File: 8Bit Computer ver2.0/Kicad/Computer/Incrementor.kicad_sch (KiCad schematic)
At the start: 13 parts, among them IC139 SN74ABT245BDWR, IC16 SN74F283D, IC42 SN74F283D, IC43 SN74AHC74DR, IC50 SN74LVC1G14DBVR, IC51 SN74LVC1G32DBVR, IC58 SN74LVC1G08DBVR, IC81 SN74F283D, IC82 SN74LVC1G14DBVR, IC83 SN74LVC1G14DBVR, IC84 SN74LVC1G86DBVR, IC87 SN74ABT574ADWR, IC88 SN74ABT574ADWR

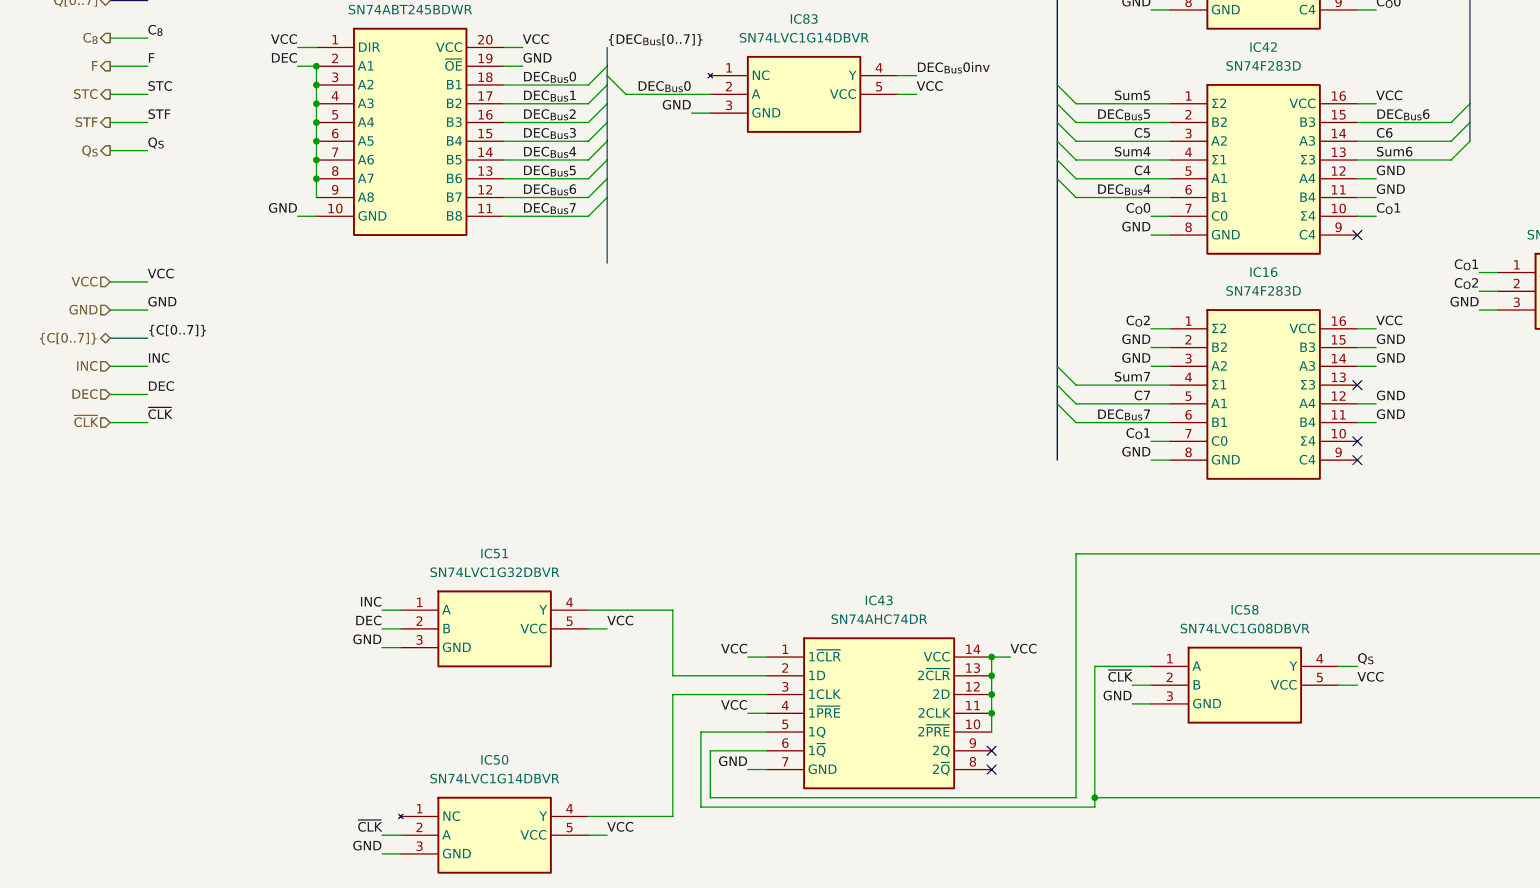
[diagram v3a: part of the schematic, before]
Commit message: Kicad
deleted the Qs
began with FlashMemory
added the CMD comparators for Inc, Comp, AddSub, FlagReg, BarrelShifter, ProgCount
added Diodes and DATdis line
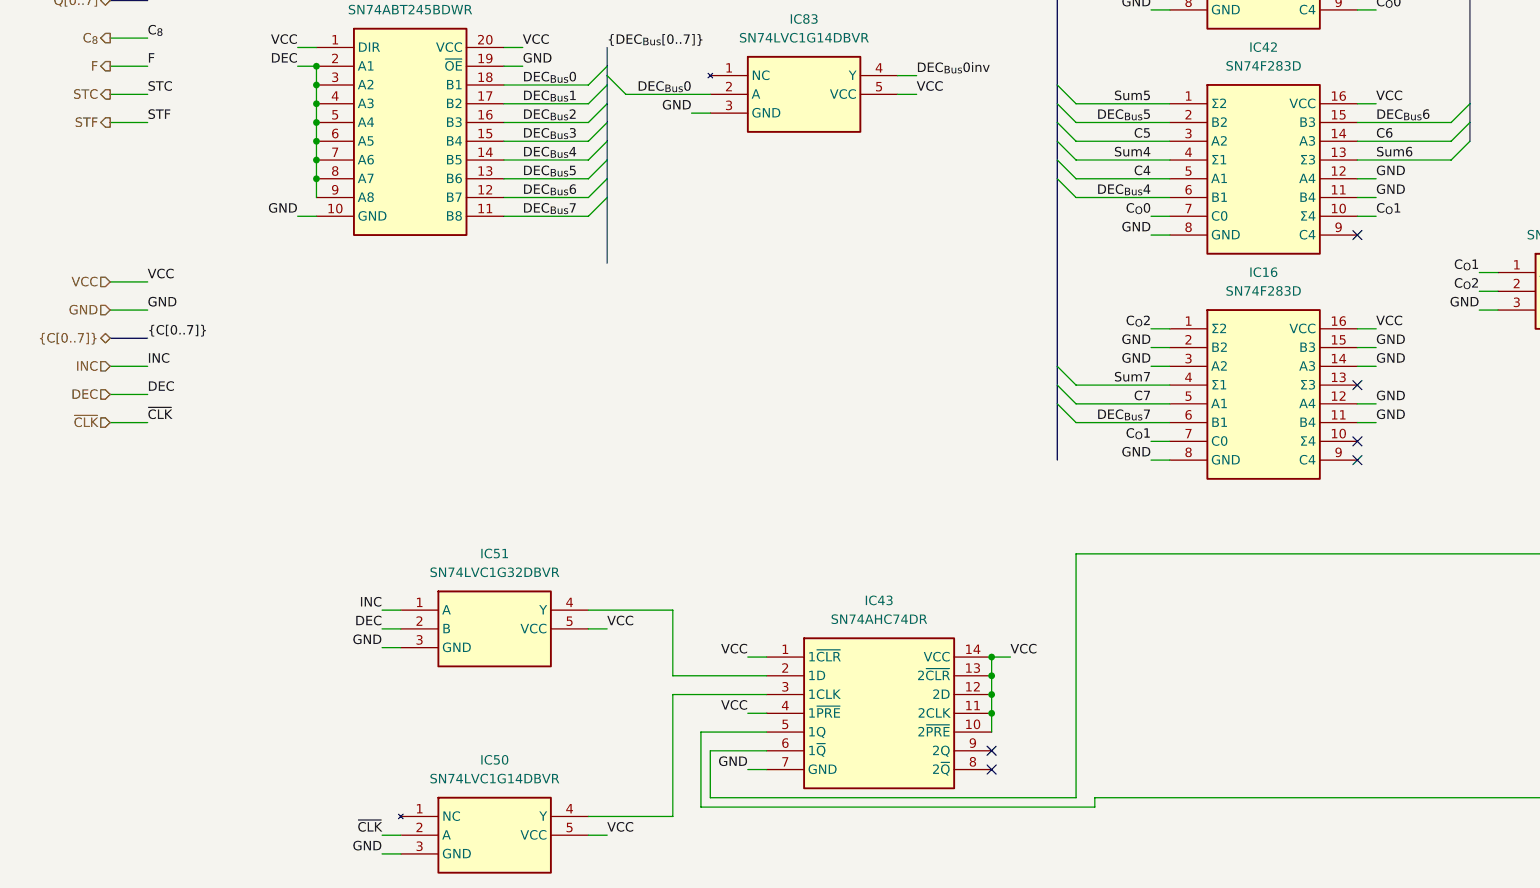
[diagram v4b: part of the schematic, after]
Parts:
- removed IC58: SN74LVC1G08DBVR, Samacsys:SOT95P280X145-5N, symbol Samacsys:SN74LVC1G08DBVR

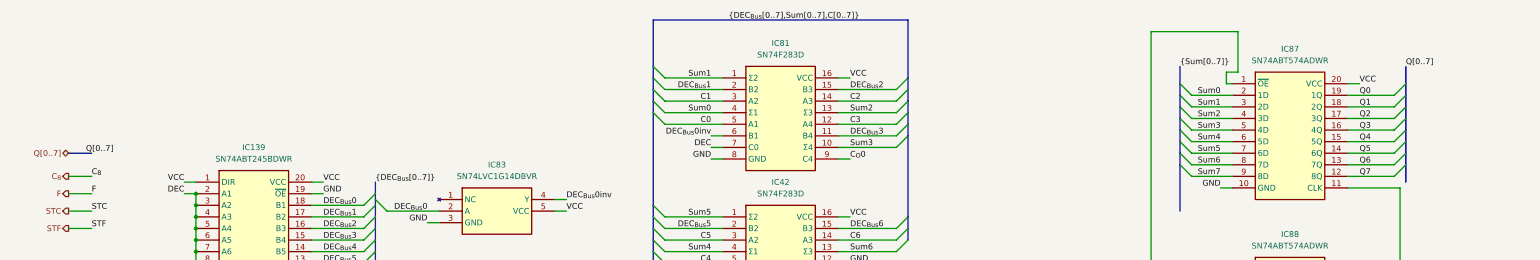
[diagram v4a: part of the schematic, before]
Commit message: Kicad, parts
Parts:
added Leds
Kicad:
added Input Output
changed Q bus to DAT bus
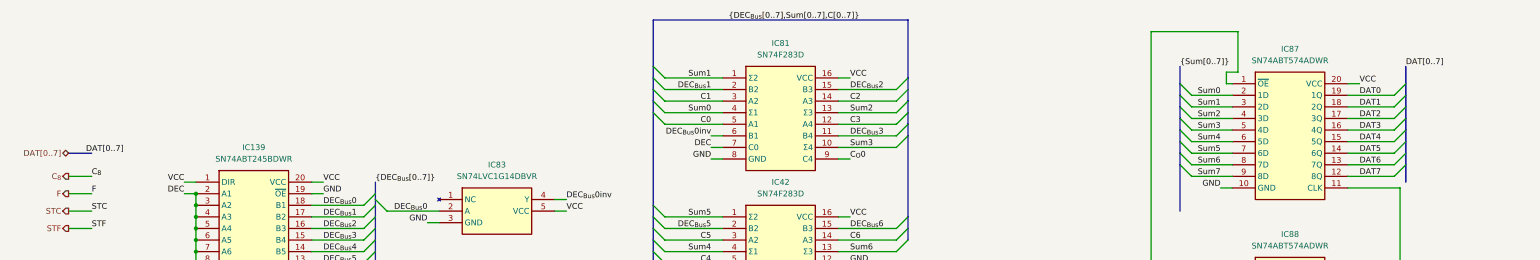
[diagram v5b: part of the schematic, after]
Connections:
- net Q0 renamed DAT0
- net Q1 renamed DAT1
- net Q2 renamed DAT2
- net Q3 renamed DAT3
- net Q4 renamed DAT4
- net Q5 renamed DAT5
- net Q6 renamed DAT6
- net Q7 renamed DAT7
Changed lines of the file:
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@@
 		)
 	)
-	(label "Q5"
+	(label "DAT5"
 		(at 306.07 60.96 0)
 		(effects
@@
 		)
 	)
-	(label "Q1"
+	(label "DAT1"
 		(at 306.07 50.8 0)
 		(effects
@@
 		)
 	)
-	(label "Q7"
+	(label "DAT7"
 		(at 306.07 66.04 0)
 		(effects
@@
 		)
 	)
-	(label "Q4"
+	(label "DAT4"
 		(at 306.07 58.42 0)
 		(effects
@@
 		)
 	)
-	(label "Q3"
+	(label "DAT3"
 		(at 306.07 55.88 0)
 		(effects
@@
 		)
 	)
-	(label "Q0"
+	(label "DAT0"
 		(at 306.07 48.26 0)
 		(effects
@@
 		)
 	)
-	(label "Q[0..7]"
+	(label "DAT[0..7]"
 		(at 316.23 41.91 0)
 		(effects
@@
 		)
 	)
-	(label "Q6"
+	(label "DAT6"
 		(at 306.07 63.5 0)
 		(effects
@@
 		)
 	)
-	(label "Q[0..7]"
+	(label "DAT[0..7]"
 		(at 26.67 60.96 0)
 		(effects
@@
 		)
 	)
-	(label "Q2"
+	(label "DAT2"
 		(at 306.07 53.34 0)
 		(effects
@@
 		)
 	)
-	(hierarchical_label "Q[0..7]"
+	(hierarchical_label "DAT[0..7]"
 		(shape tri_state)
 		(at 22.86 60.96 180)

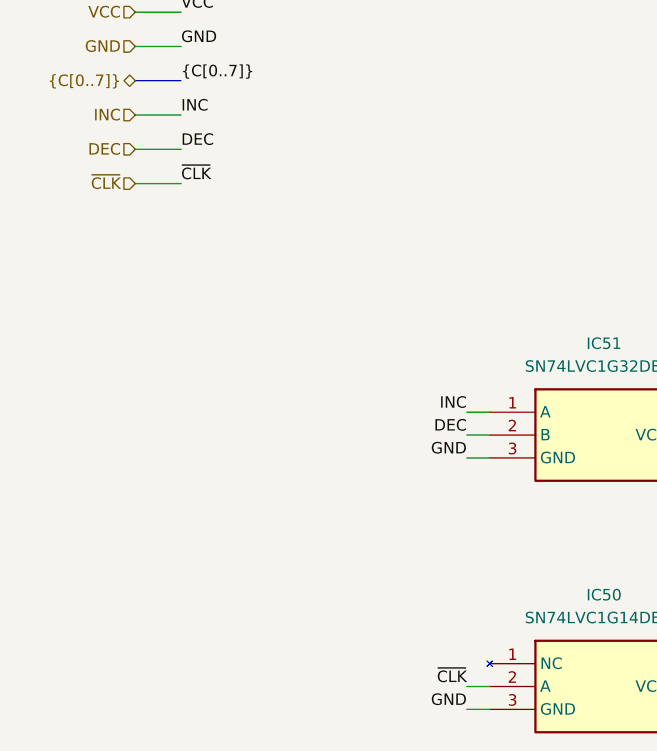
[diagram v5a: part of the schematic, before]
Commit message: Kicad, parts
parts:
added USB C PD Triggerboard
added Delay Chip for 90ns
added Push Button
Kicad:
added USB C PD Triggerboard
added rising edge detector via Delay and Xor for Accept Push Button
added VBUS net
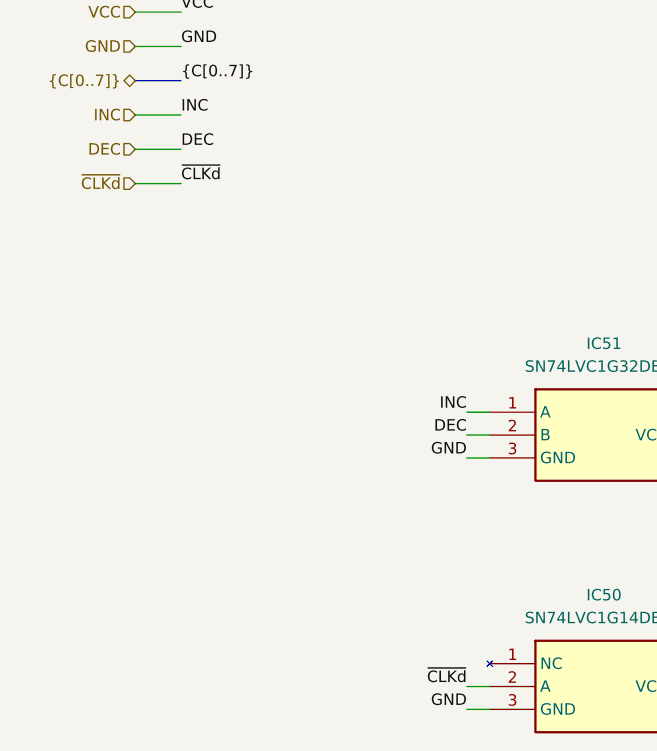
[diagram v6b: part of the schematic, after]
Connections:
- net ~{CLK} renamed ~{CLKd}
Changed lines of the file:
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@@
 		)
 	)
-	(label "~{CLK}"
+	(label "~{CLKd}"
 		(at 59.69 173.99 180)
 		(effects
@@
 		)
 	)
-	(label "~{CLK}"
+	(label "~{CLKd}"
 		(at 27.94 118.11 0)
 		(effects
@@
 		)
 	)
-	(hierarchical_label "~{CLK}"
+	(hierarchical_label "~{CLKd}"
 		(shape input)
 		(at 22.86 118.11 180)

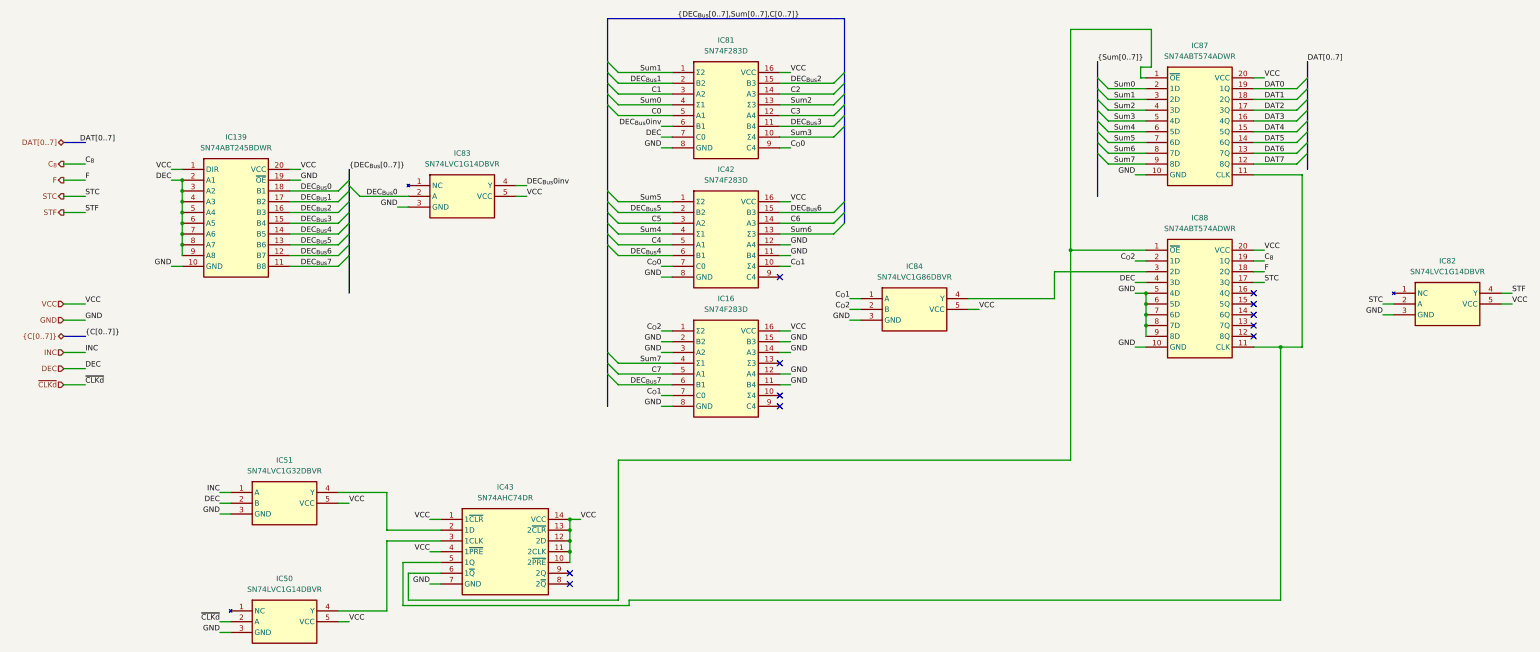
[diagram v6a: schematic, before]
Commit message: Kicad SCH/PCB
Kicad SCH/PCB:
changed the References in SCH
began with INOUTPUT module nearly done
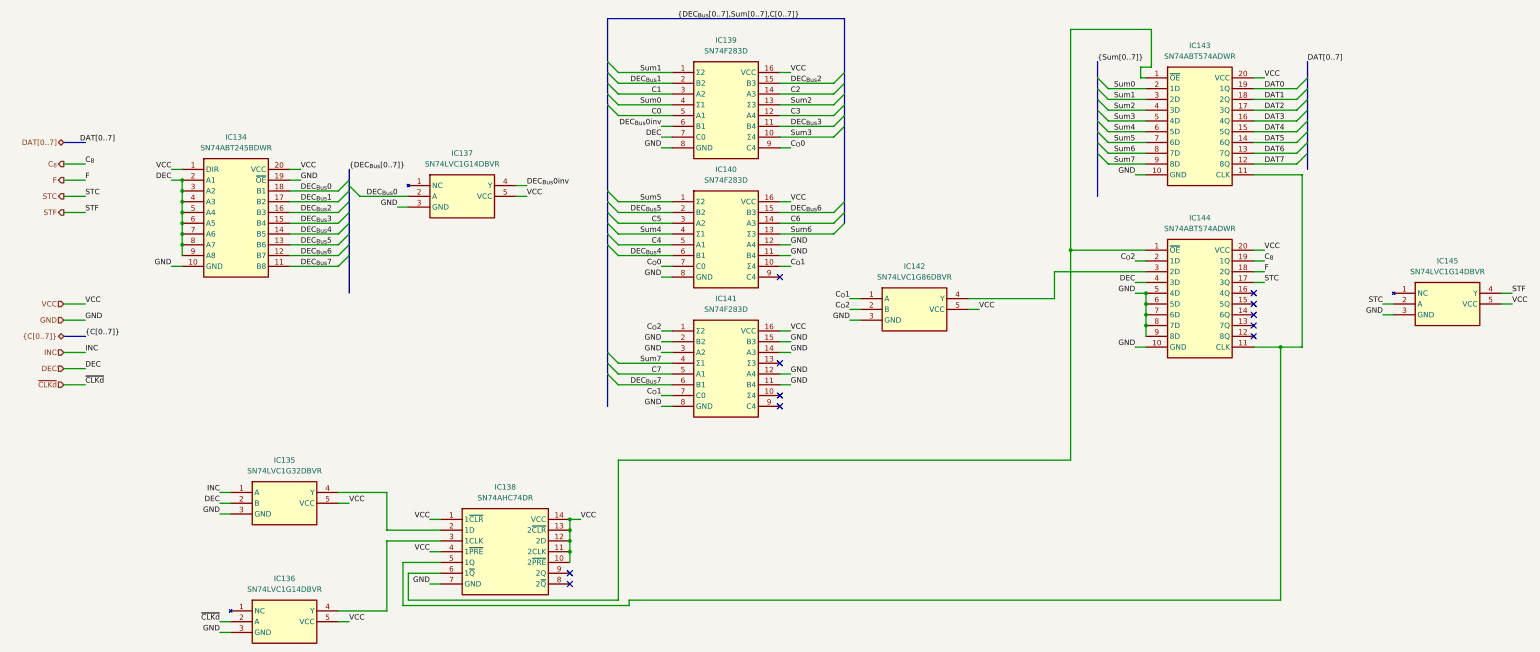
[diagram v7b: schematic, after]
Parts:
- renumbered IC139 to IC134, IC51 to IC135, IC50 to IC136, IC83 to IC137, IC43 to IC138, IC81 to IC139, IC42 to IC140, IC16 to IC141, IC84 to IC142, IC87 to IC143, IC88 to IC144, IC82 to IC145
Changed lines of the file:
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@@
 		(dnp no)
 		(fields_autoplaced yes)
-		(property "Reference" "IC51"
+		(property "Reference" "IC135"
 			(at 74.93 135.89 0)
 			(effects
@@
 			(project ""
 				(path "/1196a00e-6878-4d6d-82b7-9e052dfe7c14/c4d8b530-1c6d-45af-88d2-7dc1d4321a34/fd61ce55-ae0c-4c43-b2a6-25ced748995f"
-					(reference "IC51")
+					(reference "IC135")
 					(unit 1)
 				)
@@
 		(dnp no)
 		(fields_autoplaced yes)
-		(property "Reference" "IC16"
+		(property "Reference" "IC141"
 			(at 179.07 97.79 0)
 			(effects
@@
 			(project ""
 				(path "/1196a00e-6878-4d6d-82b7-9e052dfe7c14/c4d8b530-1c6d-45af-88d2-7dc1d4321a34/fd61ce55-ae0c-4c43-b2a6-25ced748995f"
-					(reference "IC16")
+					(reference "IC141")
 					(unit 1)
 				)
@@
 		(dnp no)
 		(fields_autoplaced yes)
-		(property "Reference" "IC83"
+		(property "Reference" "IC137"
 			(at 116.84 63.5 0)
 			(effects
@@
 			(project "Computer"
 				(path "/1196a00e-6878-4d6d-82b7-9e052dfe7c14/c4d8b530-1c6d-45af-88d2-7dc1d4321a34/fd61ce55-ae0c-4c43-b2a6-25ced748995f"
-					(reference "IC83")
+					(reference "IC137")
 					(unit 1)
 				)
@@
 		(dnp no)
 		(fields_autoplaced yes)
-		(property "Reference" "IC88"
+		(property "Reference" "IC144"
 			(at 290.83 78.74 0)
 			(effects
@@
 			(project "Computer"
 				(path "/1196a00e-6878-4d6d-82b7-9e052dfe7c14/c4d8b530-1c6d-45af-88d2-7dc1d4321a34/fd61ce55-ae0c-4c43-b2a6-25ced748995f"
-					(reference "IC88")
+					(reference "IC144")
 					(unit 1)
 				)
@@
 		(dnp no)
 		(fields_autoplaced yes)
-		(property "Reference" "IC139"
+		(property "Reference" "IC134"
 			(at 63.5 59.69 0)
 			(effects
@@
 			(project ""
 				(path "/1196a00e-6878-4d6d-82b7-9e052dfe7c14/c4d8b530-1c6d-45af-88d2-7dc1d4321a34/fd61ce55-ae0c-4c43-b2a6-25ced748995f"
-					(reference "IC139")
+					(reference "IC134")
 					(unit 1)
 				)
@@
 		(dnp no)
 		(fields_autoplaced yes)
-		(property "Reference" "IC87"
+		(property "Reference" "IC143"
 			(at 290.83 38.1 0)
 			(effects
@@
 			(project "Computer"
 				(path "/1196a00e-6878-4d6d-82b7-9e052dfe7c14/c4d8b530-1c6d-45af-88d2-7dc1d4321a34/fd61ce55-ae0c-4c43-b2a6-25ced748995f"
-					(reference "IC87")
+					(reference "IC143")
 					(unit 1)
 				)
@@
 		(dnp no)
 		(fields_autoplaced yes)
-		(property "Reference" "IC43"
+		(property "Reference" "IC138"
 			(at 127 142.24 0)
 			(effects
@@
 			(project ""
 				(path "/1196a00e-6878-4d6d-82b7-9e052dfe7c14/c4d8b530-1c6d-45af-88d2-7dc1d4321a34/fd61ce55-ae0c-4c43-b2a6-25ced748995f"
-					(reference "IC43")
+					(reference "IC138")
 					(unit 1)
 				)
@@
 		(dnp no)
 		(fields_autoplaced yes)
-		(property "Reference" "IC82"
+		(property "Reference" "IC145"
 			(at 349.25 88.9 0)
 			(effects
@@
 			(project ""
 				(path "/1196a00e-6878-4d6d-82b7-9e052dfe7c14/c4d8b530-1c6d-45af-88d2-7dc1d4321a34/fd61ce55-ae0c-4c43-b2a6-25ced748995f"
-					(reference "IC82")
+					(reference "IC145")
 					(unit 1)
 				)
@@
 		(dnp no)
 		(fields_autoplaced yes)
-		(property "Reference" "IC81"
+		(property "Reference" "IC139"
 			(at 179.07 36.83 0)
 			(effects
@@
 			(project "Computer"
 				(path "/1196a00e-6878-4d6d-82b7-9e052dfe7c14/c4d8b530-1c6d-45af-88d2-7dc1d4321a34/fd61ce55-ae0c-4c43-b2a6-25ced748995f"
-					(reference "IC81")
+					(reference "IC139")
 					(unit 1)
 				)
@@
 		(dnp no)
 		(fields_autoplaced yes)
-		(property "Reference" "IC42"
+		(property "Reference" "IC140"
 			(at 179.07 67.31 0)
 			(effects
@@
 			(project "Computer"
 				(path "/1196a00e-6878-4d6d-82b7-9e052dfe7c14/c4d8b530-1c6d-45af-88d2-7dc1d4321a34/fd61ce55-ae0c-4c43-b2a6-25ced748995f"
-					(reference "IC42")
+					(reference "IC140")
 					(unit 1)
 				)
@@
 		(dnp no)
 		(fields_autoplaced yes)
-		(property "Reference" "IC50"
+		(property "Reference" "IC136"
 			(at 74.93 163.83 0)
 			(effects
@@
 			(project ""
 				(path "/1196a00e-6878-4d6d-82b7-9e052dfe7c14/c4d8b530-1c6d-45af-88d2-7dc1d4321a34/fd61ce55-ae0c-4c43-b2a6-25ced748995f"
-					(reference "IC50")
+					(reference "IC136")
 					(unit 1)
 				)
@@
 		(dnp no)
 		(fields_autoplaced yes)
-		(property "Reference" "IC84"
+		(property "Reference" "IC142"
 			(at 223.52 90.17 0)
 			(effects
@@
 			(project ""
 				(path "/1196a00e-6878-4d6d-82b7-9e052dfe7c14/c4d8b530-1c6d-45af-88d2-7dc1d4321a34/fd61ce55-ae0c-4c43-b2a6-25ced748995f"
-					(reference "IC84")
+					(reference "IC142")
 					(unit 1)
 				)
